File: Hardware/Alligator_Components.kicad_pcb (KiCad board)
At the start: 4 copper layers, 60 x 110 mm, 114 parts, among them J1 SWD_Header, J2 Eurorack_10_pin_power, J3 Conn_01x08_Female, J4 Conn_01x08_Female, J5 Conn_01x08_Female, J6 Conn_01x08_Female, SW1 SW_SPST, SW2 SW_SPDT_MSM, U1 STM32H743ZITx, U2 IS42S16400J-xC, U3 PCM5100APW, U4 SSI2164, U5 MCP6004, U6 MCP6004, U7 TL074, U8 LM1117-3.3, Y1 8MHz 20pF

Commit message: Further updates to pcb layout
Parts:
- removed RV1: A10k, Resistors_SMD:R_0603_HandSoldering
- removed SW1: SW_SPST, Resistors_SMD:R_0603_HandSoldering
- removed SW2: SW_SPDT_MSM, Resistors_SMD:R_0603_HandSoldering
- moved C1 13.2 mm to (129.3, 103.9), turned to 270 degrees
- moved R21 4.46 mm to (129.8, 76.7), turned to 90 degrees
- moved C8 1.59 mm to (121.7, 108.8), turned to 270 degrees
- moved R43 1.49 mm to (142.4, 87.5), turned to 270 degrees
- moved C21 1.14 mm to (127.8, 103.9), turned to 270 degrees
- moved C2 1.00 mm to (139.4, 100.1)
- moved C3 0.90 mm to (129.4, 100.1)
- moved C5 0.10 mm to (136.7, 104.6)
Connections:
- J6 pad 1: /LED1 -> /DELAY_CHORUS
- J6 pad 3: /USB_VBUS -> /LED1
- J6 pad 4: /USB_DM -> /USB_DP
- J6 pad 5: /USB_DP -> /USB_DM
- J6 pad 6: /DELAY_CHORUS -> /USB_VBUS
- U1 pad 1: Net-(U1-Pad1) -> /MODE1
- U1 pad 113: Net-(U1-Pad113) -> /DELAY_CHORUS
- U1 pad 119: /DELAY_CHORUS -> Net-(U1-Pad119)
- U1 pad 2: Net-(U1-Pad2) -> /MODE2
- U1 pad 23: Net-(U1-Pad23) -> Net-(C2-Pad1)
- U1 pad 27: /MIX_WET_CTL -> Net-(U1-Pad27)
- U1 pad 34: /MIX_DRY_CTL -> /DELAY_CV_SCALED_L
- U1 pad 40: Net-(U1-Pad40) -> /MIX_DRY_CTL
- U1 pad 41: /DELAY_CV_SCALED_L -> /MIX_WET_CTL
- U1 pad 6: Net-(U1-Pad6) -> +3V3
- U1 pad 97: /MODE1 -> Net-(U1-Pad97)
- U1 pad 98: /MODE2 -> Net-(U1-Pad98)
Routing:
- net /RESET: track 0.00 -> 71.4 mm, vias 0 -> 1
- net /DELAY_POT_R: track 0.00 -> 59.1 mm
- net GND: track 15.3 -> 65.0 mm, vias 8 -> 36
- net /MODE1: track 0.00 -> 36.0 mm, vias 0 -> 1
- net /MODE2: track 0.00 -> 33.1 mm, vias 0 -> 1
- net /DAC_BCLK: track 0.00 -> 30.9 mm
- net /DELAY_CV_SCALED_L: track 35.6 -> 5.11 mm
- net +3V3: track 70.1 -> 100.1 mm, vias 8 -> 22
- net /DRY_OUT_L: track 4.66 -> 34.3 mm, vias 0 -> 2
- net /DAC_DATA: track 0.00 -> 27.8 mm, vias 0 -> 2
- net /USB_VBUS: track 0.00 -> 26.3 mm
- net /USB_DM: track 0.20 -> 24.6 mm
- net /DRY_OUT_R: track 4.66 -> 28.1 mm, vias 0 -> 2
- net /USB_DP: track 0.03 -> 22.8 mm
- net /DAC_LRCLK: track 0.00 -> 18.2 mm, vias 0 -> 2
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
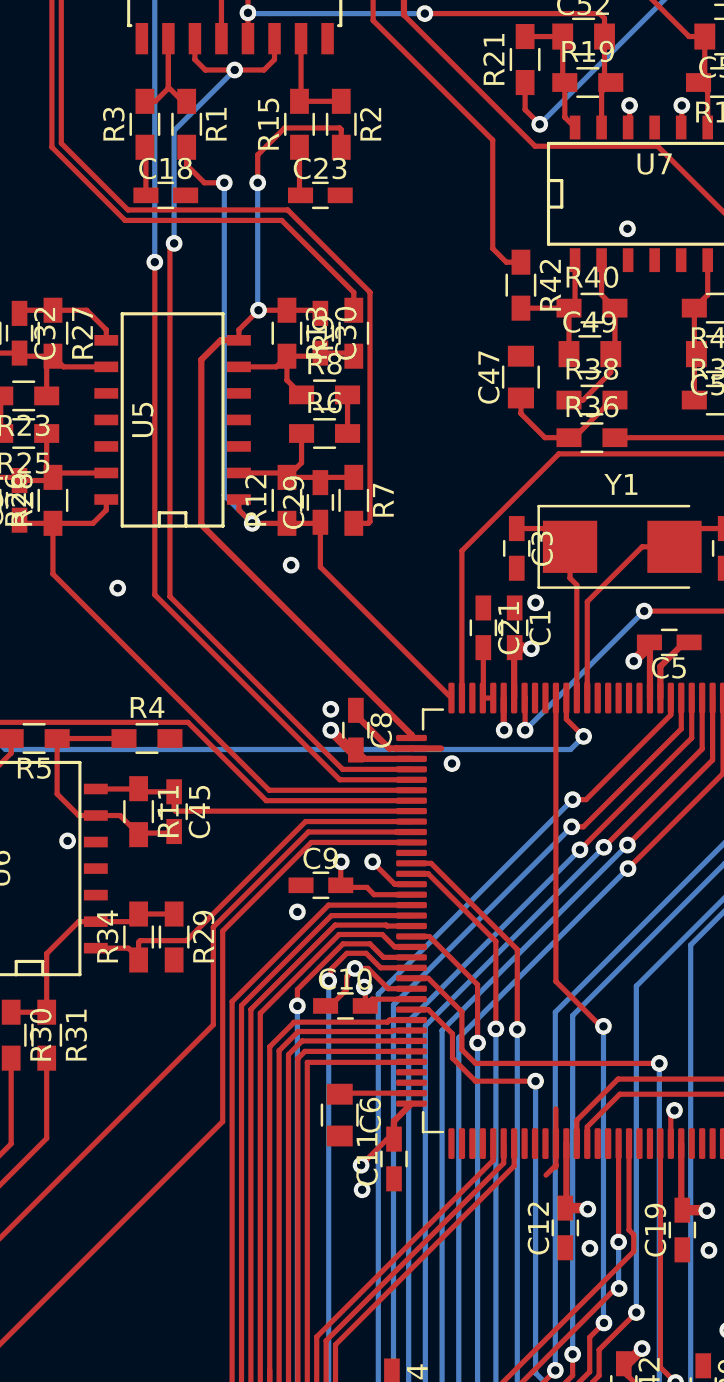
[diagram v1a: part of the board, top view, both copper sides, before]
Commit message: Error pass of schematic and PCB - power rails still need routing
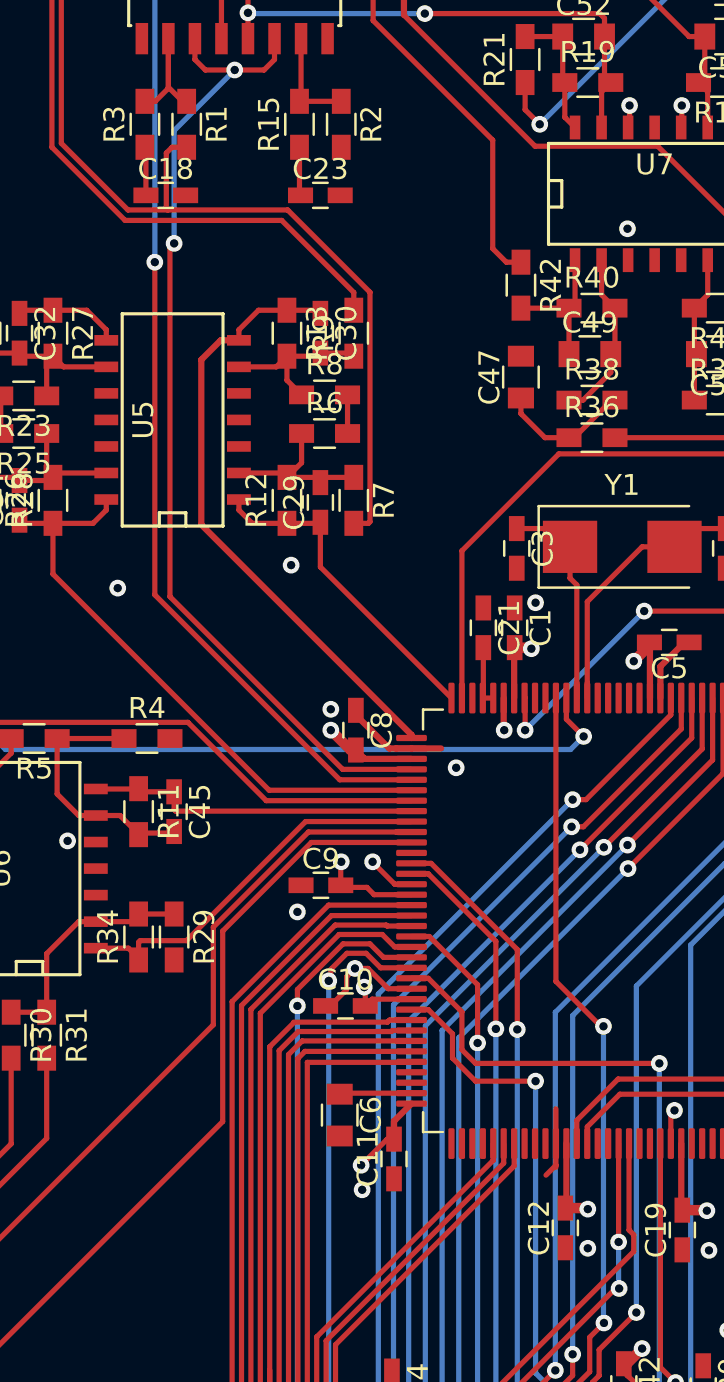
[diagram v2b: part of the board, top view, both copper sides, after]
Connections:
- R1 pad 2: /AUDIO_IN_L -> /EXT_AUDIO_IN_L
- R2 pad 2: /AUDIO_IN_R -> /EXT_AUDIO_IN_R
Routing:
- net /AUDIO_IN_L: track 35.6 -> 15.7 mm, vias 2 -> 0
- net /AUDIO_IN_R: track 42.2 -> 29.3 mm, vias 2 -> 0
- net /EXT_AUDIO_IN_L: track 46.3 -> 50.1 mm

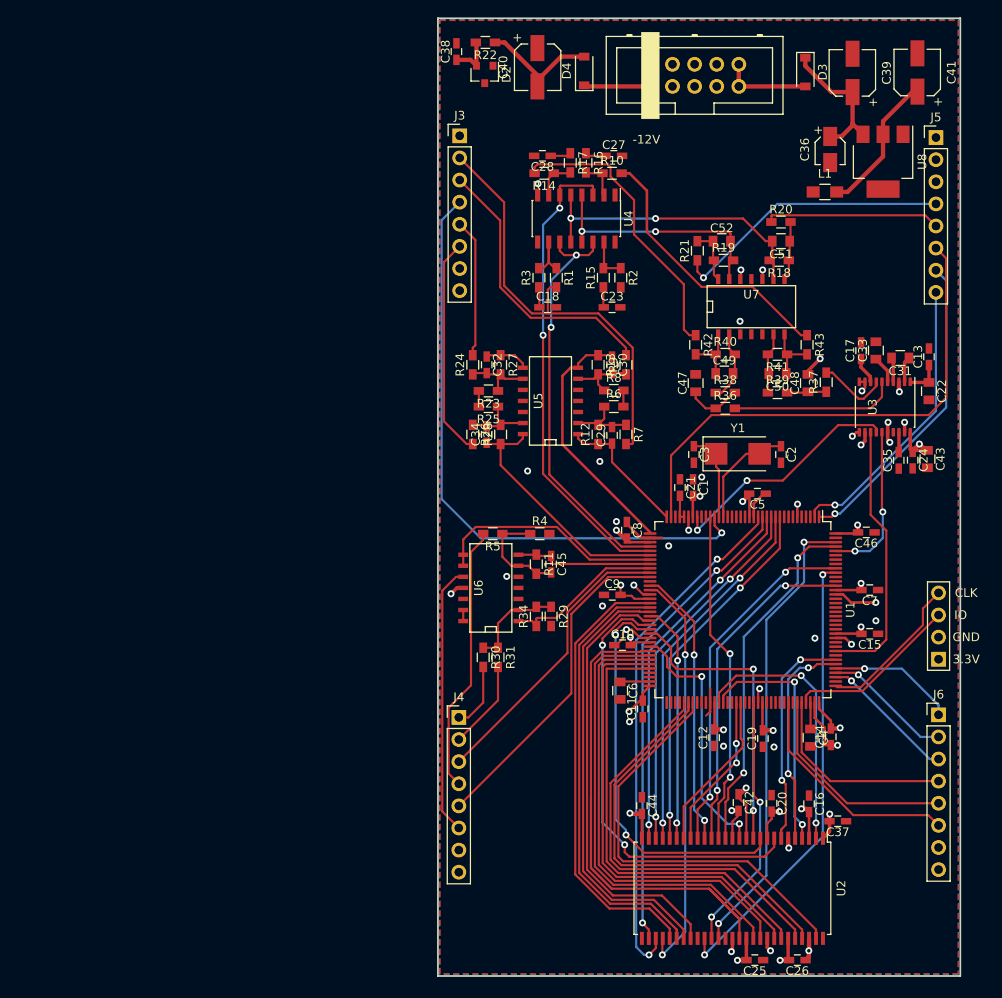
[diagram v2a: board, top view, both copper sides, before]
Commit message: Completed PCB routing
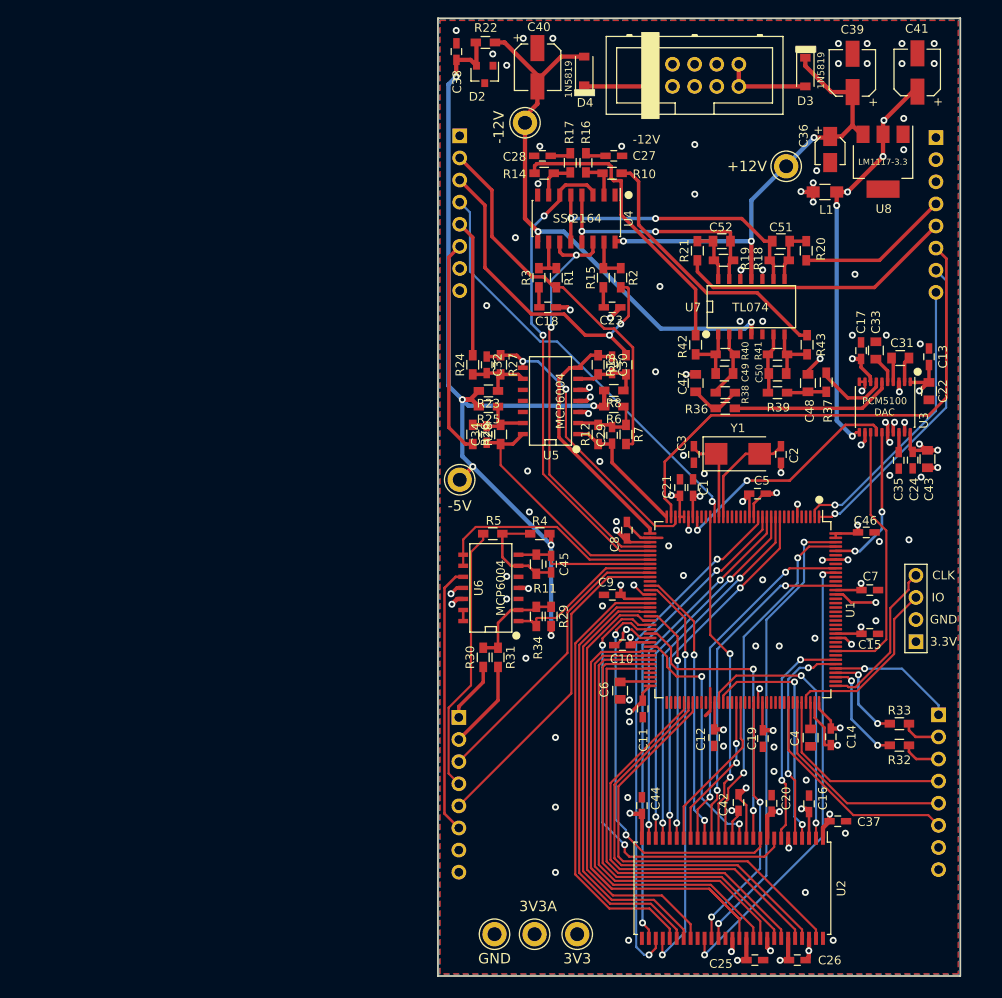
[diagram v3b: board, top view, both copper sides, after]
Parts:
- added R32: 330R, Resistors_SMD:R_0603_HandSoldering, F.Cu at (153.0, 133.5)
- added R33: 330R, Resistors_SMD:R_0603_HandSoldering, F.Cu at (153.0, 131.0)
- added TP1: TestPoint, Measurement_Points:Test_Point_Keystone_5005-5009_Compact, F.Cu at (106.5, 155.2)
- added TP2: TestPoint, Measurement_Points:Test_Point_Keystone_5005-5009_Compact, F.Cu at (116.0, 155.2)
- added TP3: TestPoint, Measurement_Points:Test_Point_Keystone_5005-5009_Compact, F.Cu at (111.1, 155.2)
- added TP4: TestPoint, Measurement_Points:Test_Point_Keystone_5005-5009_Compact, F.Cu at (102.5, 103.0)
- added TP5: TestPoint, Measurement_Points:Test_Point_Keystone_5005-5009_Compact, F.Cu at (140.0, 67.0)
- added TP6: TestPoint, Measurement_Points:Test_Point_Keystone_5005-5009_Compact, F.Cu at (110.0, 62.0)
- J3, J4, J5, J6: moved to B.Cu
- moved R20 4.39 mm to (142.3, 76.7), turned to 90 degrees
- moved J1 3.29 mm to (154.9, 121.6)
- turned J3 to 180 degrees
- turned J4 to 180 degrees
- turned J5 to 180 degrees
- turned J6 to 180 degrees
- turned R6 to 180 degrees
- turned R8 to 180 degrees
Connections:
- J3 pad 1: Net-(J3-Pad1) -> GND
- J5 pad 2: +3.3VA -> GND
- J5 pad 3: Net-(J5-Pad3) -> GND
- J5 pad 4: /EXT_AUDIO_OUT_R -> /EXT_AUDIO_OUT_L
- J5 pad 5: /EXT_AUDIO_OUT_L -> /EXT_AUDIO_OUT_R
- J6 pad 8: +3.3VA -> GND
- U1 pad 111: /LED1 -> Net-(R32-Pad2)
- U1 pad 112: /LED2 -> Net-(R33-Pad2)
- U1 pad 143: +3.3VA -> +3V3
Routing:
- net AREF_-5: track 8.94 -> 104.3 mm, vias 0 -> 6
- net /DELAY_POT_R: track 59.1 -> 111.7 mm
- net VEE: track 14.9 -> 64.9 mm, vias 0 -> 2
- net VCC: track 16.2 -> 53.0 mm, vias 0 -> 3
- net +3V3: track 100.1 -> 131.3 mm, vias 22 -> 28
- net /DELAY_CV_SCALED_L: track 5.11 -> 34.7 mm, vias 0 -> 2
- net /RESET: track 71.4 -> 49.4 mm
- net GND: track 65.0 -> 78.8 mm, vias 36 -> 98
- net Net-(R32-Pad2): track 0.00 -> 12.0 mm, vias 0 -> 2
- net +3.3VA: track 10.2 -> 21.4 mm, vias 0 -> 9
- net /LED1: track 15.7 -> 4.49 mm, vias 1 -> 0
- net Net-(R33-Pad2): track 0.00 -> 10.6 mm, vias 0 -> 2
- net /LED2: track 14.9 -> 4.47 mm, vias 1 -> 0
- net /EXT_AUDIO_IN_R: track 32.4 -> 39.1 mm, vias 0 -> 2
- net /EXT_AUDIO_IN_L: track 50.1 -> 43.9 mm
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- added copper zone on Power.Rails, net +3.3VA
- added copper zone on Power.Rails, net +3V3
- added copper zone on Ground.Fill, net GND
- removed copper zone on In2.Cu, net +3V3
- removed copper zone on In1.Cu, net GND
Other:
- board text added: "+12V"
- board text added: "-12V"
- board text added: "-5V"
- board text added: "3V3"
- board text added: "3V3A"
- board text added: "GND"
- board text added: "PCM5100 DAC"

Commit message: Components first draft done; Started Controls PCB; Gerber and SMT assembly tests
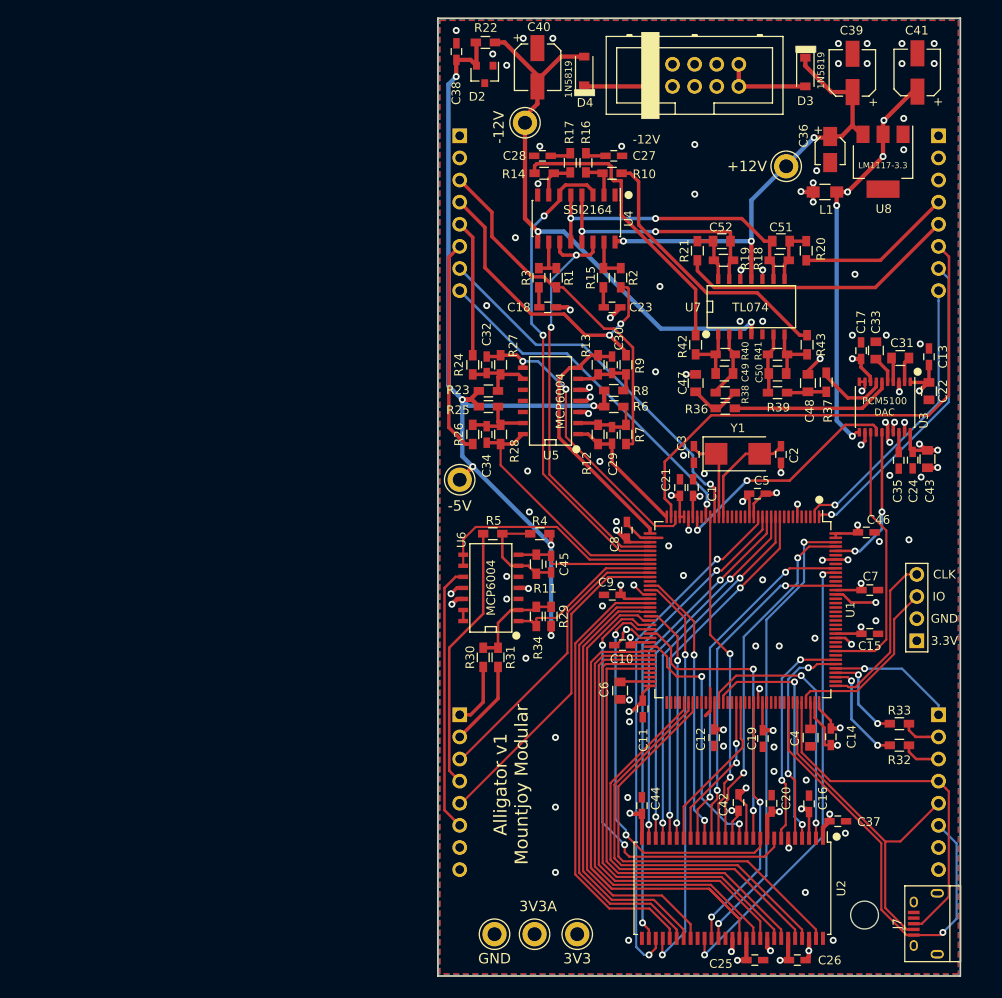
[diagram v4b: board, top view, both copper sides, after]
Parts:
- added H1: MountingHole_Pad, Mounting_Holes:MountingHole_3.2mm_M3, F.Cu at (149.0, 153.0)
- added J7: USB_B_Micro, Custom_Footprints:USB_Micro-B_Amphenol, F.Cu at (156.0, 154.0)
- J3, J4, J5, J6: footprint Socket_Strips:Socket_Strip_Straight_1x08_Pitch2.54mm -> Pin_Headers:Pin_Header_Straight_1x08_Pitch2.54mm
- R22: value 2.2k -> 2k2
- moved J5 0.36 mm to (157.5, 63.5)
- moved J4 0.32 mm to (102.5, 130.0)
- moved J1 0.14 mm to (155.0, 121.5)
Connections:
- J3 pad 1: GND -> +3.3VA
- J3 pad 2: /EXT_AUDIO_IN_L -> GND
- J3 pad 3: /EXT_AUDIO_IN_R -> /EXT_AUDIO_IN_L
- J3 pad 4: /RESET -> /EXT_AUDIO_IN_R
- J3 pad 7: GND -> /RESET
- J3 pad 8: +3.3VA -> /TONE_POT
- U1 pad 27: Net-(U1-Pad27) -> /TONE_POT
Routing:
- net /DELAY_POT_R: track 111.7 -> 60.0 mm
- net /TONE_POT: track 0.00 -> 40.8 mm, vias 0 -> 1
- net /USB_VBUS: track 26.3 -> 50.4 mm, vias 0 -> 1
- net /USB_DP: track 22.8 -> 41.9 mm
- net /USB_DM: track 24.6 -> 40.3 mm
- net /RESET: track 49.4 -> 44.1 mm
- net /EXT_AUDIO_IN_R: track 39.1 -> 36.5 mm
- net /EXT_AUDIO_IN_L: track 43.9 -> 41.4 mm
- net /SWCLK: track 18.0 -> 18.9 mm
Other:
- board text added: "Alligator v1 Mountjoy Modular"

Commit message: Tooling holes added for SMT assembly; started routing control PCB
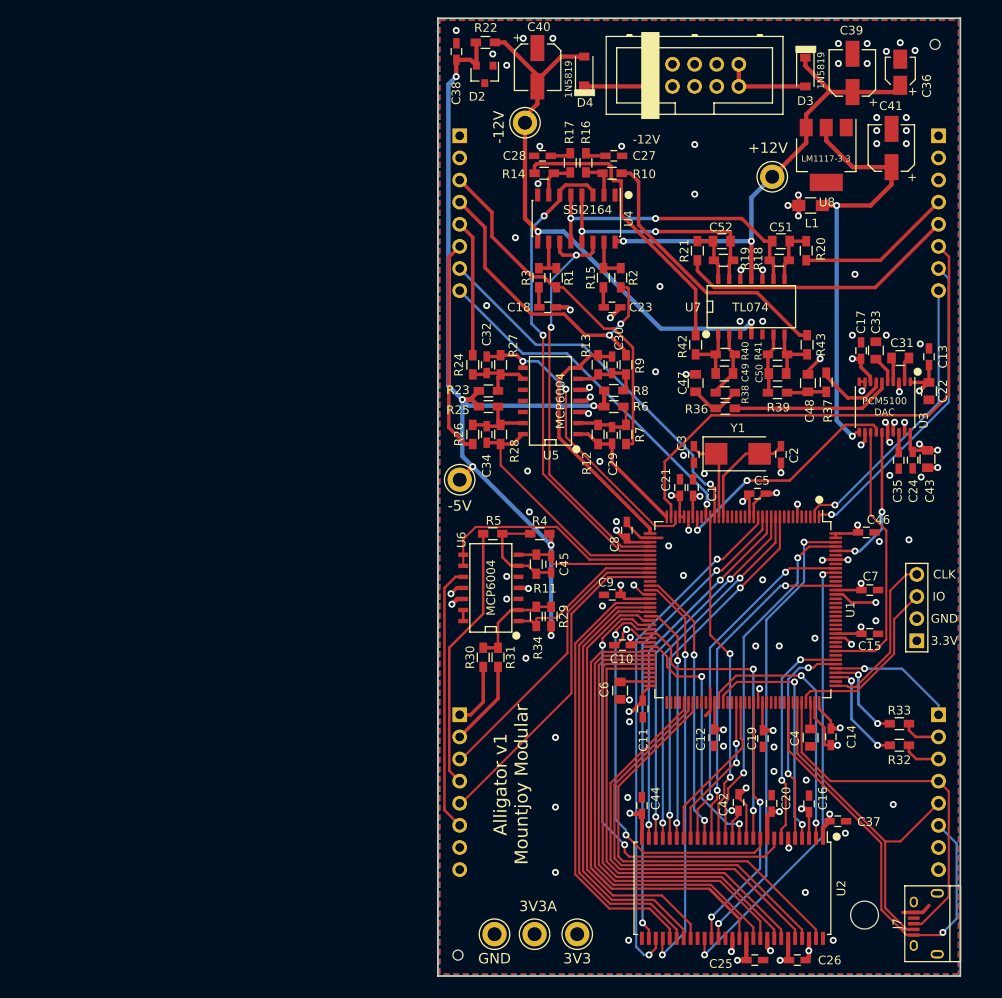
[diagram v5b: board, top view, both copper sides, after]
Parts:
- added JLC_Tooling: MountingHole_2.2mm_M2, Mounting_Holes:MountingHole_2.2mm_M2, F.Cu at (102.3, 157.6)
- added JLC_Tooling: MountingHole_2.2mm_M2, Mounting_Holes:MountingHole_2.2mm_M2, F.Cu at (157.1, 53.0)
- moved C36 12.0 mm to (153.1, 56.2), turned to 90 degrees
- moved C41 9.17 mm to (152.1, 64.9)
- moved U8 6.57 mm to (144.6, 65.7)
- moved L1 2.26 mm to (142.8, 71.5)
- moved TP5 2.00 mm to (138.4, 68.2)
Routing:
- net VCC: track 53.0 -> 57.0 mm, vias 3 -> 2
- net GND: track 78.8 -> 82.2 mm, vias 98 -> 101
- net +3V3: track 131.3 -> 134.5 mm, vias 28 -> 25
